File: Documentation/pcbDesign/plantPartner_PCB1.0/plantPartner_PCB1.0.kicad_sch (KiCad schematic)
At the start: 26 parts, among them IC1 MPM3610, J1 Conn_01x04, J2 Conn_01x04, J3 Conn_01x04, J4 Screw_Terminal, J5 Screw_Terminal, J6 Screw_Terminal, U1 ESP32-WROOM-32, U2 MAX485

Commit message: Prototype demo changes. Small things for testing
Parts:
- added J7: Conn_01x03, symbol Connector_Generic:Conn_01x03
- added K1: SRD-12VDC-SL-C, SRD-12VDC-SL-C:RELAY_SRD-12VDC-SL-C, symbol SRD-12VDC-SL-C:SRD-12VDC-SL-C
- added R12, R13, R14, R15: R, Resistor_SMD:R_0201_0603Metric, symbol Device:R
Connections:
- net GND: now also J7.1 (Pin_1), K1.COIL2
- net NC: now reaches J6.1 (Pin_1)
- net NC: now also K1.NC
- net COM: now reaches J6.2 (Pin_2)
- net COM: now also K1.COM
- net NO: now reaches J6.3 (Pin_3)
- net NO: now also K1.NO
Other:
- note added: "12V Relay - Unfinished"
- moved on the sheet: EL1, J5, J6

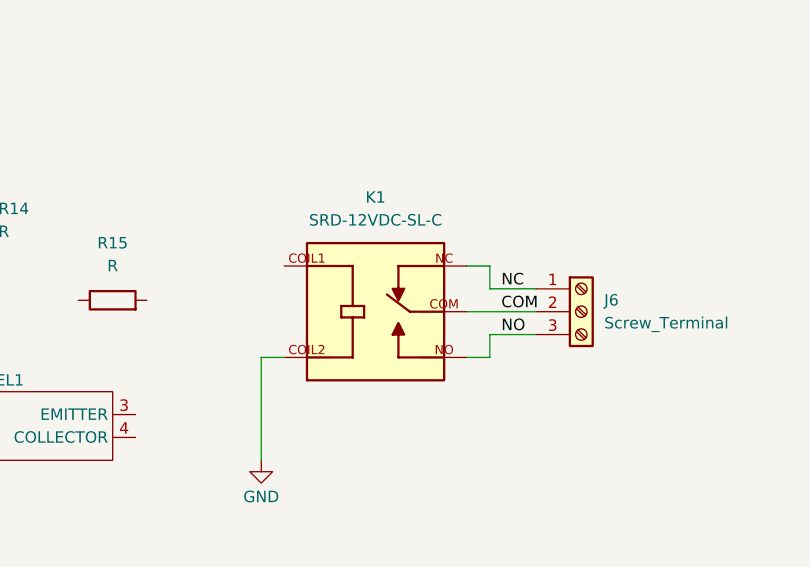
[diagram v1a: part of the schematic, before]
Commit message: Working on relay
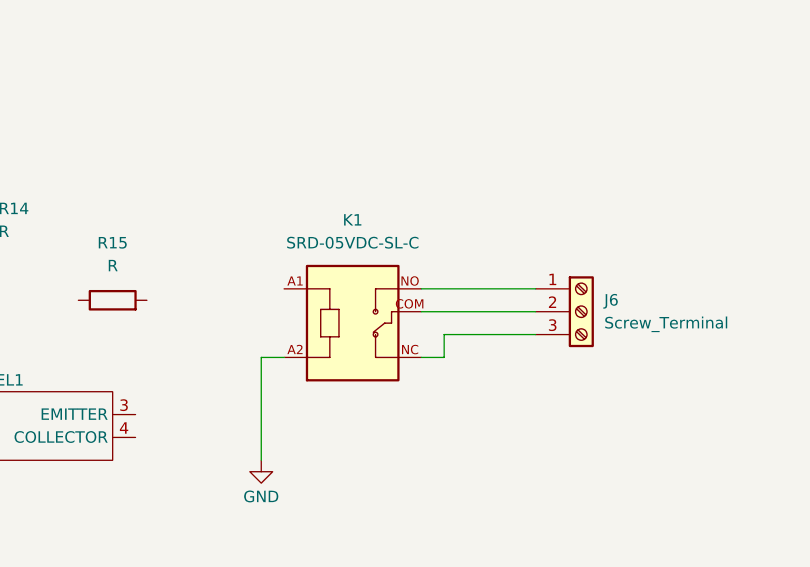
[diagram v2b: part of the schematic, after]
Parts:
- removed K1: SRD-12VDC-SL-C, SRD-12VDC-SL-C:RELAY_SRD-12VDC-SL-C, symbol SRD-12VDC-SL-C:SRD-12VDC-SL-C
- added K1: SRD-05VDC-SL-C, SRD-05VDC-SL-C:RELAY_SRD-05VDC-SL-C, symbol SRD-05VDC-SL-C:SRD-05VDC-SL-C
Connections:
- net GND: now also K1.A2
- net COM: no longer names the net of J6.2 (Pin_2)
- net COM: now also K1.COM
- net NC: no longer names the net of J6.1 (Pin_1)
- net NC: now also K1.NO
- net NO: no longer names the net of J6.3 (Pin_3)
- net NO: now also K1.NC

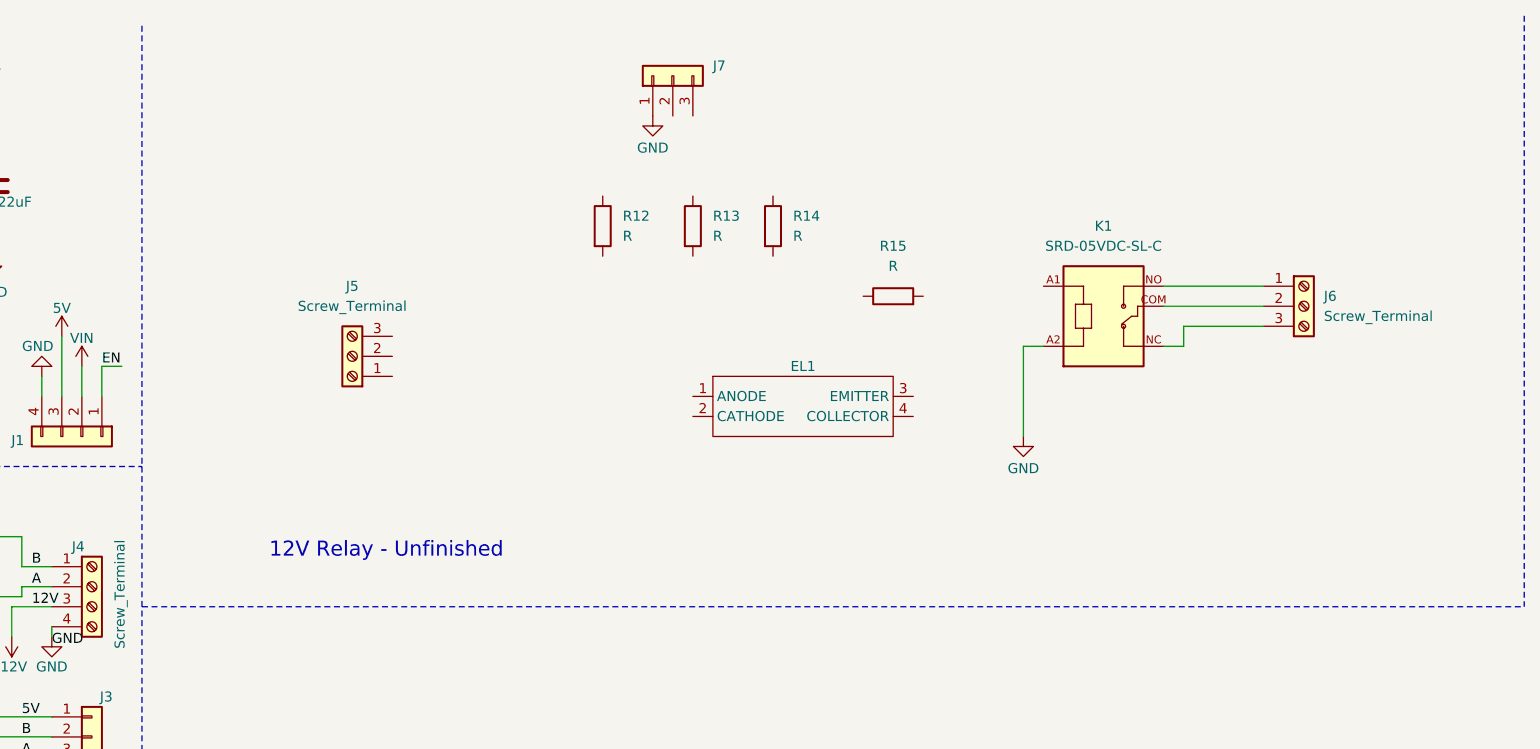
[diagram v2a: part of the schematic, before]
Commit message: Implemented 5V Relay to our specs. Time to verify it and add AC to 12V Adapter to overall schematic then draw PCB
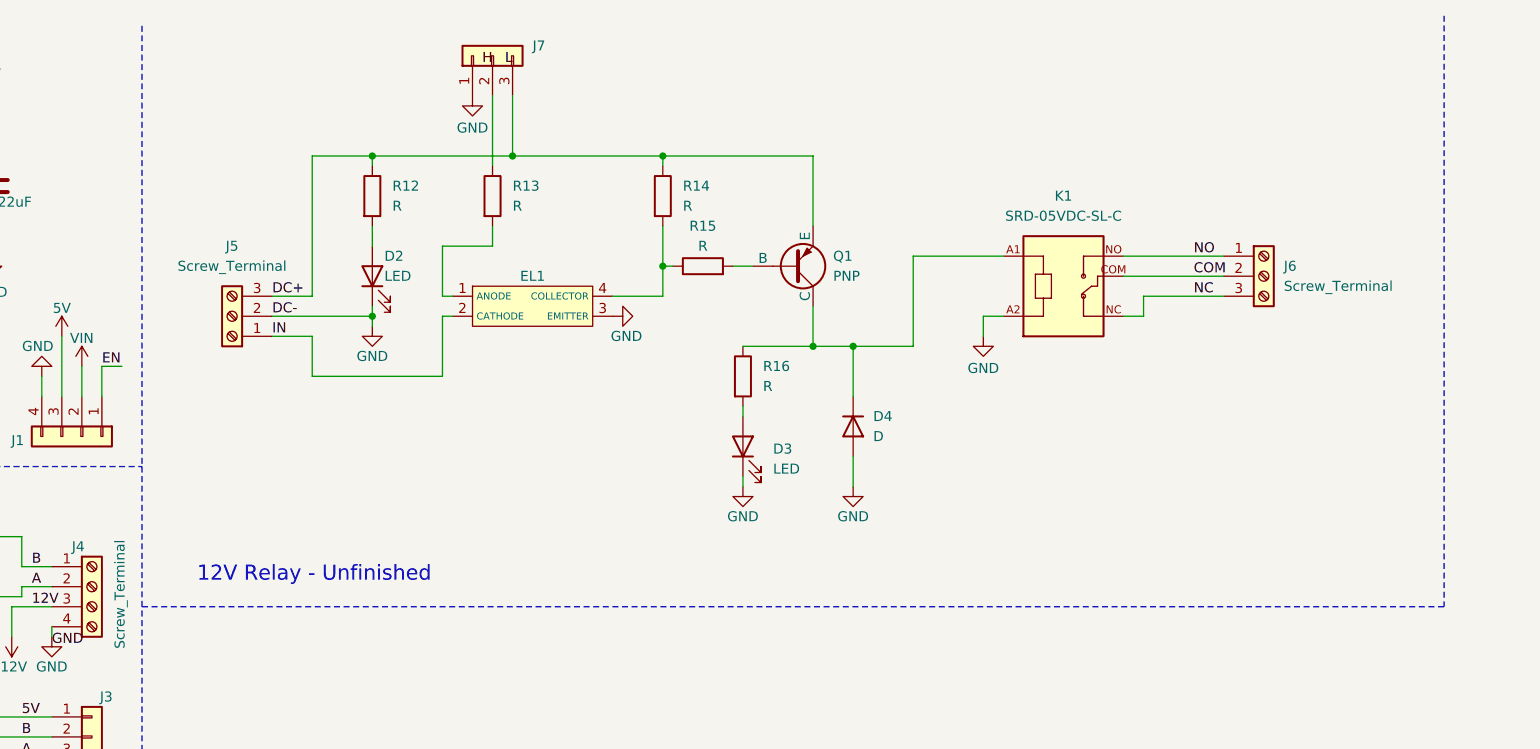
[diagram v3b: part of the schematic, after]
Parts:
- added D2, D3: LED, symbol Device:LED
- added D4: D, symbol Device:D
- added Q1: PNP, symbol Simulation_SPICE:PNP
- added R16: R, symbol Device:R
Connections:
- net 12V: now also EL1.2 (CATHODE), J5.1 (Pin_1)
- net GND: now also EL1.3 (EMITTER), J5.2 (Pin_2), D2.1 (K), D3.1 (K), D4.2 (A)
- net DC+: now reaches J5.3 (Pin_3)
- net DC+: now also J7.3 (Pin_3), R12.1, R14.1, Q1.3 (E)
- net at R12.2: now also D2.2 (A)
- net at R15.1: now also EL1.4 (COLLECTOR), R14.2
- net at R15.2: now also Q1.2 (B)
- net at J7.2 (Pin_2): now also R13.1
- net at EL1.1 (ANODE): now also R13.2
- net at K1.A1: now also D4.1 (K), Q1.1 (C), R16.1
- net COM: now reaches J6.2 (Pin_2), K1.COM
- net NC: now reaches J6.3 (Pin_3), K1.NC
- net NO: now reaches J6.1 (Pin_1), K1.NO
- new net: D3.2 (A), R16.2
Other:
- moved on the sheet: J5, J6, J7, K1, R12, R13, R14, R15

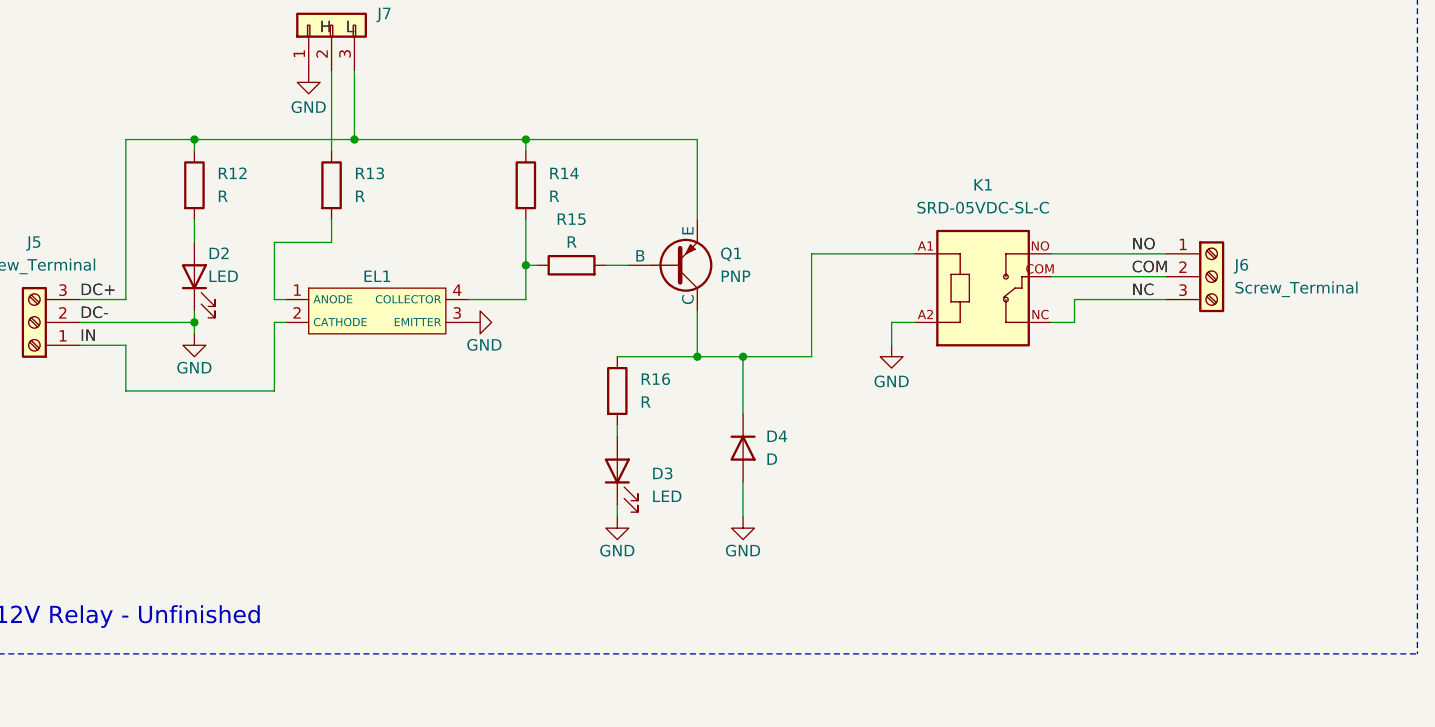
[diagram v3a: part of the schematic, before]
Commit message: Inserting resistor values and symbol footprints to 5V relay schematic
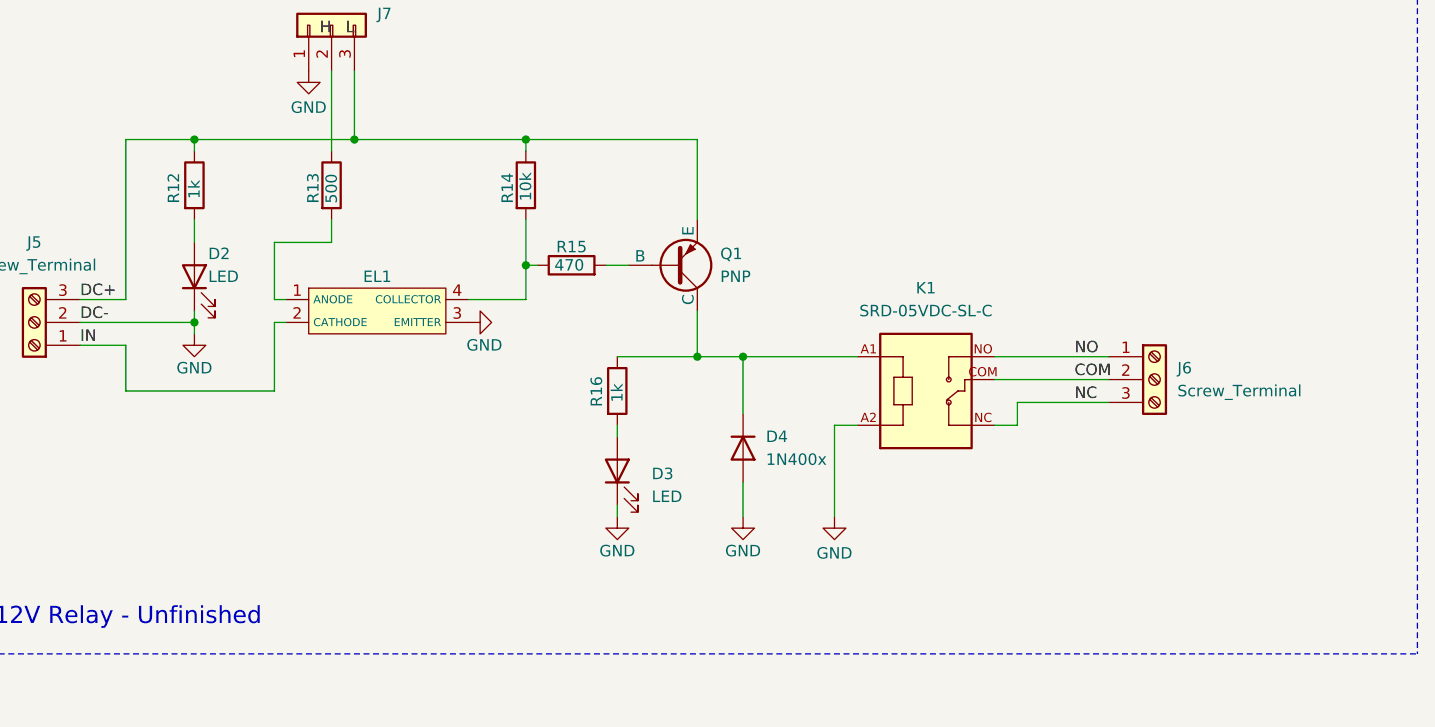
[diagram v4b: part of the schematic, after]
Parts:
- D2, D3: footprint (none) -> LED_SMD:LED_0201_0603Metric
- D4: value D -> 1N400x; footprint (none) -> Diode_THT:D_A-405_P7.62mm_Horizontal
- R12, R16: value R -> 1k
- R13: value R -> 500
- R14: value R -> 10k
- R15: value R -> 470
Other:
- moved on the sheet: J6, K1
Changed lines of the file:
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@@
 	(wire
 		(pts
-			(xy 236.22 43.18) (xy 248.92 43.18)
+			(xy 229.87 54.61) (xy 242.57 54.61)
 		)
 		(stroke
@@
 	(wire
 		(pts
-			(xy 220.98 50.8) (xy 218.44 50.8)
-		)
-		(stroke
-			(width 0)
-			(type default)
-		)
-	)
-	(wire
-		(pts
 			(xy 201.93 68.58) (xy 201.93 72.39)
 		)
@@
 	(wire
 		(pts
-			(xy 209.55 54.61) (xy 201.93 54.61)
+			(xy 201.93 54.61) (xy 214.63 54.61)
 		)
 		(stroke
@@
 	(wire
 		(pts
-			(xy 220.98 43.18) (xy 209.55 43.18)
-		)
-		(stroke
-			(width 0)
-			(type default)
-		)
-	)
-	(wire
-		(pts
 			(xy 201.93 54.61) (xy 201.93 60.96)
 		)
@@
 	(wire
 		(pts
-			(xy 236.22 45.72) (xy 248.92 45.72)
+			(xy 229.87 57.15) (xy 242.57 57.15)
 		)
 		(stroke
@@
 	(wire
 		(pts
-			(xy 218.44 50.8) (xy 218.44 53.34)
-		)
-		(stroke
-			(width 0)
-			(type default)
-		)
-	)
-	(wire
-		(pts
 			(xy 187.96 71.12) (xy 187.96 72.39)
 		)
@@
 	(wire
 		(pts
-			(xy 238.76 48.26) (xy 238.76 50.8)
+			(xy 232.41 59.69) (xy 232.41 62.23)
 		)
 		(stroke
@@
 	(wire
 		(pts
-			(xy 238.76 48.26) (xy 248.92 48.26)
-		)
-		(stroke
-			(width 0)
-			(type default)
-		)
-	)
-	(wire
-		(pts
-			(xy 209.55 43.18) (xy 209.55 54.61)
+			(xy 232.41 59.69) (xy 242.57 59.69)
 		)
 		(stroke
@@
 	(wire
 		(pts
+			(xy 212.09 62.23) (xy 214.63 62.23)
+		)
+		(stroke
+			(width 0)
+			(type default)
+		)
+	)
+	(wire
+		(pts
 			(xy 186.69 44.45) (xy 189.23 44.45)
 		)
@@
 	(wire
 		(pts
+			(xy 212.09 62.23) (xy 212.09 72.39)
+		)
+		(stroke
+			(width 0)
+			(type default)
+		)
+	)
+	(wire
+		(pts
 			(xy 25.4 41.91) (xy 35.56 41.91)
 		)
@@
 	(wire
 		(pts
-			(xy 238.76 50.8) (xy 236.22 50.8)
+			(xy 232.41 62.23) (xy 229.87 62.23)
 		)
 		(stroke
@@
 	)
 	(label "NC"
-		(at 245.11 48.26 0)
+		(at 238.76 59.69 0)
 		(effects
 			(font
@@
 	)
 	(label "NO"
-		(at 245.11 43.18 0)
+		(at 238.76 54.61 0)
 		(effects
 			(font
@@
 	)
 	(label "COM"
-		(at 245.11 45.72 0)
+		(at 238.76 57.15 0)
 		(effects
 			(font
@@
 		(on_board yes)
 		(dnp no)
-		(fields_autoplaced yes)
 		(property "Reference" "R16"
-			(at 190.5 57.1499 0)
+			(at 185.674 60.198 90)
 			(effects
 				(font
@@
 			)
 		)
-		(property "Value" "R"
-			(at 190.5 59.6899 0)
+		(property "Value" "1k"
+			(at 187.96 59.69 90)
 			(effects
 				(font
@@
 		(on_board yes)
 		(dnp no)
-		(fields_autoplaced yes)
 		(property "Reference" "R12"
-			(at 143.51 34.2899 0)
+			(at 138.684 37.592 90)
 			(effects
 				(font
@@
 			)
 		)
-		(property "Value" "R"
-			(at 143.51 36.8299 0)
+		(property "Value" "1k"
+			(at 140.97 37.084 90)
 			(effects
 				(font
@@
 			)
 		)
-		(property "Footprint" ""
+		(property "Footprint" "LED_SMD:LED_0201_0603Metric"
 			(at 187.96 67.31 0)
 			(effects
@@
 			)
 		)
-		(property "Value" "D"
+		(property "Value" "1N400x"
 			(at 204.47 66.0399 90)
 			(effects
@@
 			)
 		)
-		(property "Footprint" ""
+		(property "Footprint" "Diode_THT:D_A-405_P7.62mm_Horizontal"
 			(at 201.93 64.77 0)
 			(effects
@@
 		(dnp no)
 		(property "Reference" "R15"
-			(at 182.88 39.37 90)
+			(at 182.88 42.418 90)
 			(effects
 				(font
@@
 			)
 		)
-		(property "Value" "R"
-			(at 182.88 41.91 90)
+		(property "Value" "470"
+			(at 182.626 44.45 90)
 			(effects
 				(font
@@
 	(symbol
 		(lib_id "power:GND")
-		(at 218.44 53.34 0)
+		(at 212.09 72.39 0)
 		(unit 1)
 		(exclude_from_sim no)
@@
 		(dnp no)
 		(property "Reference" "#PWR020"
-			(at 218.44 59.69 0)
+			(at 212.09 78.74 0)
 			(effects
 				(font
@@
 		)
 		(property "Value" "GND"
-			(at 218.44 57.404 0)
+			(at 212.09 76.454 0)
 			(effects
 				(font
@@
 		)
 		(property "Footprint" ""
-			(at 218.44 53.34 0)
+			(at 212.09 72.39 0)
 			(effects
 				(font
@@
 		)
 		(property "Datasheet" ""
-			(at 218.44 53.34 0)
+			(at 212.09 72.39 0)
 			(effects
 				(font
@@
 		)
 		(property "Description" "Power symbol creates a global label with name \"GND\" , ground"
-			(at 218.44 53.34 0)
+			(at 212.09 72.39 0)
 			(effects
 				(font
@@
 		(on_board yes)
 		(dnp no)
-		(fields_autoplaced yes)
 		(property "Reference" "R13"
-			(at 158.75 34.2899 0)
+			(at 154.178 37.592 90)
 			(effects
 				(font
@@
 			)
 		)
-		(property "Value" "R"
-			(at 158.75 36.8299 0)
+		(property "Value" "500"
+			(at 156.21 37.592 90)
 			(effects
 				(font
@@
 			)
 		)
-		(property "Footprint" ""
+		(property "Footprint" "LED_SMD:LED_0201_0603Metric"
 			(at 140.97 45.72 0)
 			(effects
@@
 	(symbol
 		(lib_id "SRD-05VDC-SL-C:SRD-05VDC-SL-C")
-		(at 228.6 45.72 0)
+		(at 222.25 57.15 0)
 		(unit 1)
 		(exclude_from_sim no)
@@
 		(fields_autoplaced yes)
 		(property "Reference" "K1"
-			(at 228.6 35.56 0)
+			(at 222.25 46.99 0)
 			(effects
 				(font
@@
 		)
 		(property "Value" "SRD-05VDC-SL-C"
-			(at 228.6 38.1 0)
+			(at 222.25 49.53 0)
 			(effects
 				(font
@@
 		)
 		(property "Footprint" "SRD-05VDC-SL-C:RELAY_SRD-05VDC-SL-C"
-			(at 228.6 45.72 0)
+			(at 222.25 57.15 0)
 			(effects
 				(font
@@
 		)
 		(property "Datasheet" ""
-			(at 228.6 45.72 0)
+			(at 222.25 57.15 0)
 			(effects
 				(font
@@
 		)
 		(property "Description" ""
-			(at 228.6 45.72 0)
+			(at 222.25 57.15 0)
 			(effects
 				(font
@@
 		)
 		(property "MF" "Songle Relay"
-			(at 228.6 45.72 0)
+			(at 222.25 57.15 0)
 			(effects
 				(font
@@
 		)
 		(property "Description_1" "5V Trigger Relay Module For Arduino And Raspberry Pi 5V Trigger Relay Module For Arduino And Raspberry Pi"
-			(at 228.6 45.72 0)
+			(at 222.25 57.15 0)
 			(effects
 				(font
@@
 		)
 		(property "Package" "NON STANDARD-5 Songle Relay"
-			(at 228.6 45.72 0)
+			(at 222.25 57.15 0)
 			(effects
 				(font
@@
 		)
 		(property "Price" "None"
-			(at 228.6 45.72 0)
+			(at 222.25 57.15 0)
 			(effects
 				(font
@@
 		)
 		(property "Check_prices" "https://www.snapeda.com/parts/SRD-05VDC-SL-C/Songle+Relay/view-part/?ref=eda"
-			(at 228.6 45.72 0)
+			(at 222.25 57.15 0)
 			(effects
 				(font
@@
 		)
 		(property "STANDARD" "IPC-7251"
-			(at 228.6 45.72 0)
+			(at 222.25 57.15 0)
 			(effects
 				(font
@@
 		)
 		(property "SnapEDA_Link" "https://www.snapeda.com/parts/SRD-05VDC-SL-C/Songle+Relay/view-part/?ref=snap"
-			(at 228.6 45.72 0)
+			(at 222.25 57.15 0)
 			(effects
 				(font
@@
 		)
 		(property "MP" "SRD-05VDC-SL-C"
-			(at 228.6 45.72 0)
+			(at 222.25 57.15 0)
 			(effects
 				(font
@@
 		)
 		(property "Availability" "In Stock"
-			(at 228.6 45.72 0)
+			(at 222.25 57.15 0)
 			(effects
 				(font
@@
 		)
 		(property "MANUFACTURER" "SONGLE RELAY"
-			(at 228.6 45.72 0)
+			(at 222.25 57.15 0)
 			(effects
 				(font
@@
 		(on_board yes)
 		(dnp no)
-		(fields_autoplaced yes)
 		(property "Reference" "R14"
-			(at 180.34 34.2899 0)
+			(at 175.768 37.592 90)
 			(effects
 				(font
@@
 			)
 		)
-		(property "Value" "R"
-			(at 180.34 36.8299 0)
+		(property "Value" "10k"
+			(at 177.8 37.338 90)
 			(effects
 				(font
@@
 	(symbol
 		(lib_id "Connector:Screw_Terminal_01x03")
-		(at 254 45.72 0)
+		(at 247.65 57.15 0)
 		(unit 1)
 		(exclude_from_sim no)
@@
 		(fields_autoplaced yes)
 		(property "Reference" "J6"
-			(at 256.54 44.4499 0)
+			(at 250.19 55.8799 0)
 			(effects
 				(font
@@
 		)
 		(property "Value" "Screw_Terminal"
-			(at 256.54 46.9899 0)
+			(at 250.19 58.4199 0)
 			(effects
 				(font
@@
 		)
 		(property "Footprint" "TerminalBlock_Phoenix:TerminalBlock_Phoenix_MKDS-1,5-3-5.08_1x03_P5.08mm_Horizontal"
-			(at 254 45.72 0)
+			(at 247.65 57.15 0)
 			(effects
 				(font
@@
 		)
 		(property "Datasheet" "~"
-			(at 254 45.72 0)
+			(at 247.65 57.15 0)
 			(effects
 				(font
@@
 		)
 		(property "Description" "Generic screw terminal, single row, 01x03, script generated (kicad-library-utils/schlib/autogen/connector/)"
-			(at 254 45.72 0)
+			(at 247.65 57.15 0)
 			(effects
 				(font
